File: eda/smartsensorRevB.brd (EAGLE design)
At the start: 47 x 26.7 mm, 33 parts, among them Q1 MOSFET-NCHANNELSMD, Q2 MOSFET-NCHANNELSMD, Q3 MOSFET-NCHANNELSMD, Q4 MOSFET-NCHANNELSMD, U1 ISL83491SOIC, U2 ATTINY1634

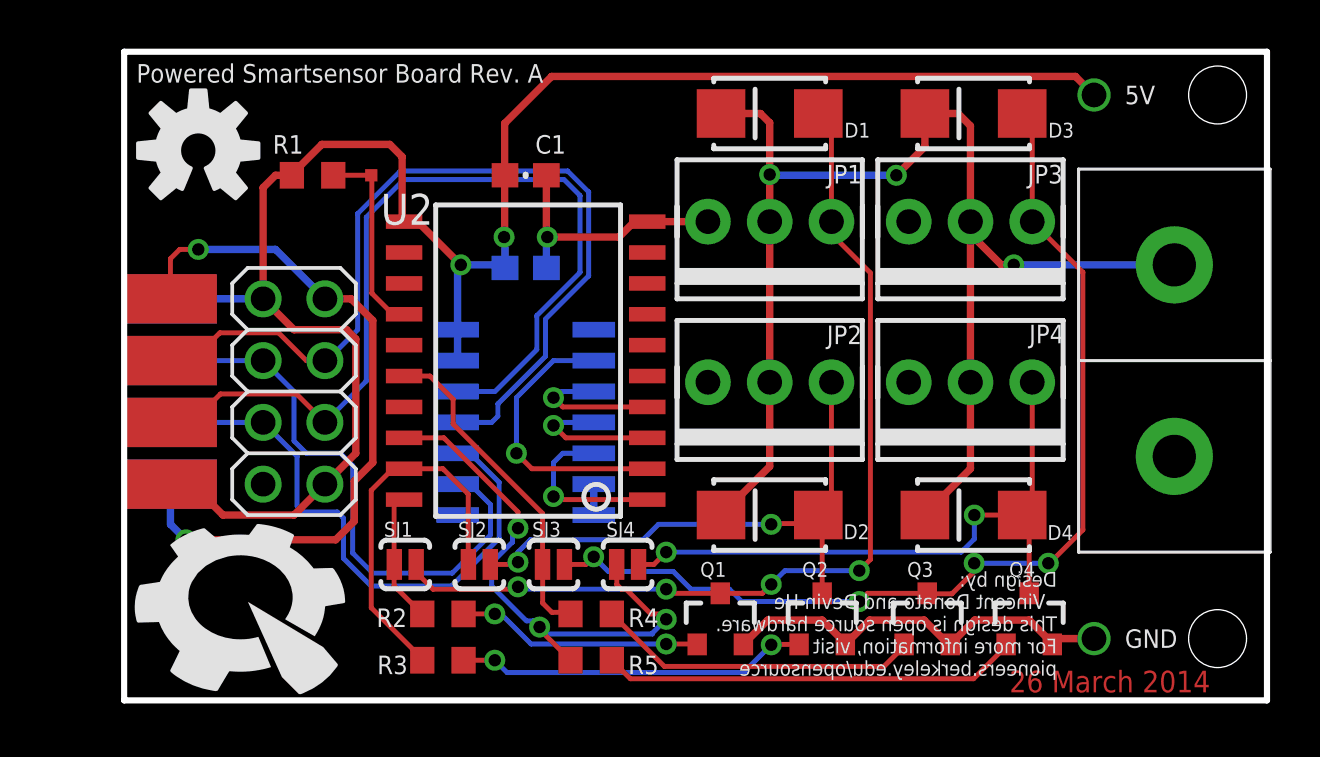
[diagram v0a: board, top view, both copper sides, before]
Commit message: Add a significantly smaller version of the (unpowered) smartsensor board.
Labels are currently out of whack and will be fixed in a future commit.

Change-Id: Iec70f93029498c3404d22c51049da2227b03999d
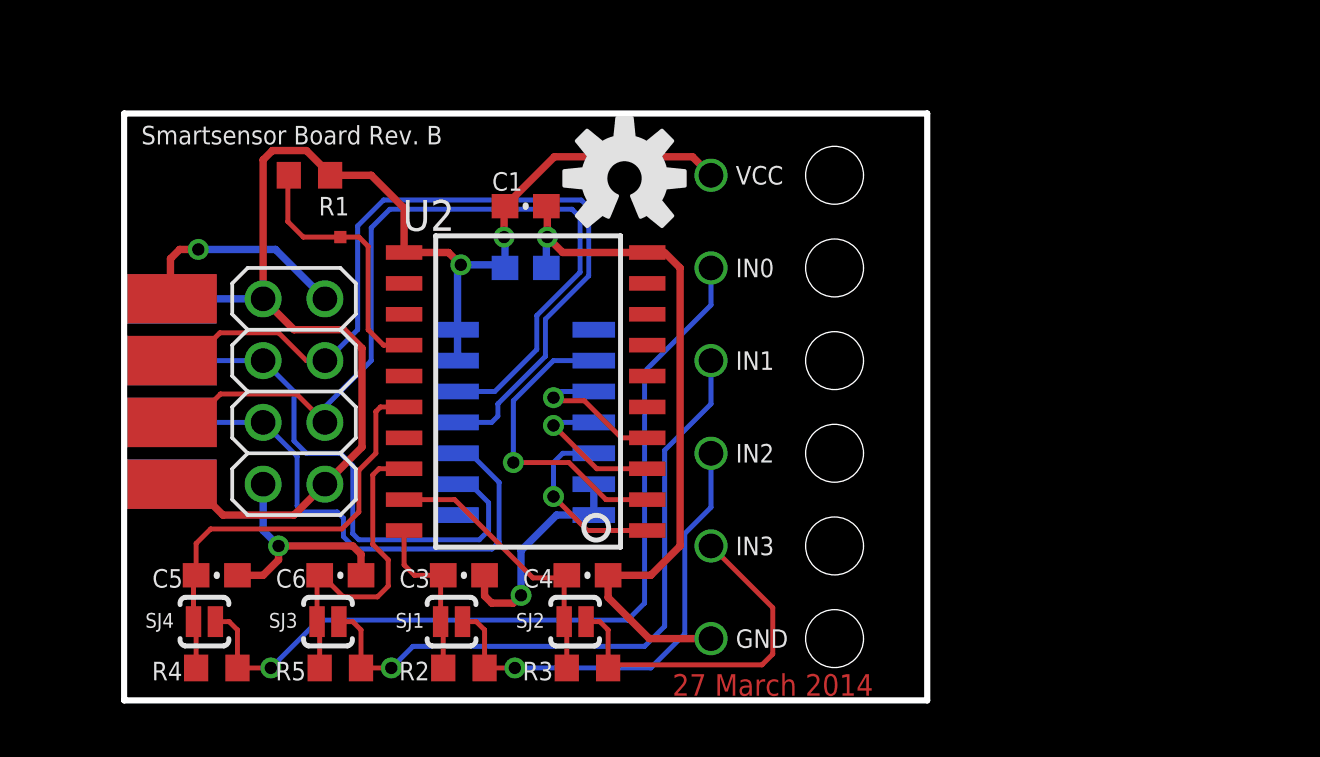
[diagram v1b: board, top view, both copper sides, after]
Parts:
- removed 5V: WIRE_WITH_HOLE, pie:WIRE_WITH_HOLE
- removed CONN1: ANDERSONVERTICAL, pie:ANDERSON_VERTICAL
- removed D1, D2, D3, D4: (no value), pie:SMA-DIODE_ALT
- removed JP1, JP2, JP3, JP4: (no value), pie:1X03-MTA
- removed Q1, Q2, Q3, Q4: MOSFET-NCHANNELSMD, pie:SOT23-3
- added C3, C4, C5, C6: (no value), pie:0603-CAP
- added IN0, IN1, IN2, IN3, VCC: WIRE_WITH_HOLE, pie:WIRE_WITH_HOLE
- R2, R3, R4, R5: value 1k -> (none)
- moved U$10 17.6 mm to (20.6, 21.5)
- moved SJ4 17.6 mm to (3.30, 3.24), turned to 180 degrees
- moved GND 15.7 mm to (26.7, 2.54)
- moved R4 15.6 mm to (3.81, 1.33), turned to 180 degrees
- moved R5 10.3 mm to (8.89, 1.33), turned to 180 degrees
- moved SJ3 9.56 mm to (8.38, 3.24), turned to 180 degrees
- moved R3 5.95 mm to (19.1, 1.33), turned to 180 degrees
- moved SJ2 4.58 mm to (18.5, 3.24), turned to 180 degrees
- moved SJ1 3.02 mm to (13.5, 3.24), turned to 180 degrees
- moved TP1 2.84 mm to (8.89, 19.1)
- moved R2 2.38 mm to (14.0, 1.33), turned to 180 degrees
- moved U2 1.27 mm to (20.3, 6.35)
- moved C1 1.27 mm to (16.5, 20.3)
- moved U$1 0.68 mm to (4.45, 4.32), flipped to the bottom
- moved R1 0.13 mm to (7.62, 21.6), turned to 0 degrees
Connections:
- removed net N$1: D1.A, JP1.1, Q1.3, SJ1.2
- removed net N$10: D4.A, JP4.1, Q4.3, SJ4.2
- removed net N$11: Q4.1, R5.2
- removed net N$2: Q1.1, R2.2
- removed net N$4: D2.A, JP2.1, Q2.3, SJ2.2
- removed net N$5: Q2.1, R3.2
- removed net N$7: D3.A, JP3.1, Q3.3, SJ3.2
- removed net N$8: Q3.1, R4.2
- removed net VCC: CONN1.PIN2, D1.C, D2.C, D3.C, D4.C, JP1.2, JP2.2, JP3.2, JP4.2
- new net CONN1: IN2.P$1, R2.1, SJ1.1
- new net CONN2: IN3.P$1, R3.1, SJ2.1
- new net CONN3: IN0.P$1, R4.1, SJ4.1
- new net CONN4: IN1.P$1, R5.1, SJ3.1
- net 5V: now also VCC.P$1; no longer 5V.P$1
- net GND: now also C3.1, C4.2, C5.2, C6.2; no longer CONN1.PIN1, JP1.3, JP2.3, JP3.3, JP4.3, Q1.2, Q2.2, Q3.2, Q4.2
- net IO1: now also C3.2, R2.2, SJ1.2; no longer R2.1, SJ1.1
- net IO2: now also C4.1, R3.2, SJ2.2; no longer R3.1, SJ2.1
- net IO3: now also C5.1, R4.2, SJ4.2; no longer R4.1, SJ3.1
- net IO4: now also C6.1, R5.2, SJ3.2; no longer R5.1, SJ4.1
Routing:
- net VCC: track 56.0 -> 0.00 mm, vias 3 -> 0
- net N$7: track 41.8 -> 0.00 mm, vias 4 -> 0
- net N$1: track 39.3 -> 0.00 mm, vias 4 -> 0
- net CONN3: track 0.00 -> 35.4 mm, vias 0 -> 1
- net CONN4: track 0.00 -> 27.5 mm, vias 0 -> 1
- net N$10: track 26.2 -> 0.00 mm, vias 2 -> 0
- net N$4: track 23.4 -> 0.00 mm, vias 2 -> 0
- net CONN1: track 0.00 -> 19.3 mm, vias 0 -> 1
- net 5V: track 76.9 -> 57.9 mm
- net N$11: track 17.2 -> 0.00 mm
- net CONN2: track 0.00 -> 15.4 mm
- net N$5: track 14.5 -> 0.00 mm, vias 2 -> 0
- net N$8: track 13.3 -> 0.00 mm
- net N$2: track 10.3 -> 0.00 mm, vias 2 -> 0
- net IO4: track 23.4 -> 13.5 mm, vias 3 -> 0
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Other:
- board size 47 x 26.7 mm -> 33 x 24.1 mm
- board text added: "27 March 2014"
- board text added: "Smartsensor Board Rev. B"
- board text removed: "26 March 2014"
- board text removed: "Powered Smartsensor Board Rev. A"
